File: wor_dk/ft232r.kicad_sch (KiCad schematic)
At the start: 18 parts, among them J401 USB_C_Receptacle_USB2.0_14P, U401 FT232RL

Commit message: wor_dk: add footprints & part info for all capacitors
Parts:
- C401: footprint Capacitor_SMD:C_0201_0603Metric -> Capacitor_SMD:C_0805_2012Metric; Comment (none) -> JLCPCB basic part; LCSC C85930 -> C1710; MPN (none) -> CL21B103KBANNNC; Manufacturer Murata Electronics -> Samsung Electro-Mechanics
- C402, C404: MPN (none) -> GRM033R61E104KE14D
- C403: MPN (none) -> CL10A475KO8NNNC
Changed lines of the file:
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@@
 			)
 		)
-		(property "Footprint" "Capacitor_SMD:C_0201_0603Metric"
+		(property "Footprint" "Capacitor_SMD:C_0805_2012Metric"
 			(at 127.9652 69.85 0)
 			(effects
@@
 			)
 		)
-		(property "Datasheet" "~"
+		(property "Datasheet" "https://wmsc.lcsc.com/wmsc/upload/file/pdf/v2/lcsc/2304140030_Samsung-Electro-Mechanics-CL21B103KBANNNC_C1710.pdf"
 			(at 127 66.04 0)
 			(effects
@@
 			)
 		)
-		(property "Description" "25V 10nF X7R ±10% 0201"
+		(property "Description" "50V 10nF X7R ±10% 0805 MLCC"
 			(at 127 66.04 0)
 			(effects
@@
 			)
 		)
-		(property "LCSC" "C85930"
+		(property "LCSC" "C1710"
 			(at 127 66.04 0)
 			(effects
@@
 			)
 		)
-		(property "Manufacturer" "Murata Electronics"
+		(property "Manufacturer" "Samsung Electro-Mechanics"
 			(at 127 66.04 0)
 			(effects
@@
 		)
 		(property "Part Number" "GRM033R71E103KE14D"
+			(at 127 66.04 0)
+			(effects
+				(font
+					(size 1.27 1.27)
+				)
+				(hide yes)
+			)
+		)
+		(property "Comment" "JLCPCB basic part"
+			(at 127 66.04 0)
+			(effects
+				(font
+					(size 1.27 1.27)
+				)
+				(hide yes)
+			)
+		)
+		(property "MPN" "CL21B103KBANNNC"
 			(at 127 66.04 0)
 			(effects
@@
 			)
 		)
-		(property "Datasheet" "~"
+		(property "Datasheet" "https://wmsc.lcsc.com/wmsc/upload/file/pdf/v2/lcsc/1811081532_Murata-Electronics-GRM033R61E104KE14D_C76939.pdf"
 			(at 154.94 86.36 0)
 			(effects
@@
 		)
 		(property "Part Number" "GRM033R61E104KE14D"
+			(at 154.94 86.36 0)
+			(effects
+				(font
+					(size 1.27 1.27)
+				)
+				(hide yes)
+			)
+		)
+		(property "MPN" "GRM033R61E104KE14D"
 			(at 154.94 86.36 0)
 			(effects
@@
 			)
 		)
-		(property "Datasheet" "~"
+		(property "Datasheet" "https://wmsc.lcsc.com/wmsc/upload/file/pdf/v2/lcsc/1811081532_Murata-Electronics-GRM033R61E104KE14D_C76939.pdf"
 			(at 153.67 66.04 0)
 			(effects
@@
 		)
 		(property "Part Number" "GRM033R61E104KE14D"
+			(at 153.67 66.04 0)
+			(effects
+				(font
+					(size 1.27 1.27)
+				)
+				(hide yes)
+			)
+		)
+		(property "MPN" "GRM033R61E104KE14D"
 			(at 153.67 66.04 0)
 			(effects
@@
 			)
 		)
-		(property "Datasheet" "~"
+		(property "Datasheet" "https://wmsc.lcsc.com/wmsc/upload/file/pdf/v2/lcsc/2304140030_Samsung-Electro-Mechanics-CL10A475KO8NNNC_C19666.pdf"
 			(at 167.64 66.04 0)
 			(effects
@@
 			(at 167.64 66.04 0)
 			(effects
+				(font
+					(size 1.27 1.27)
+				)
+				(hide yes)
+			)
+		)
+		(property "MPN" "CL10A475KO8NNNC"
+			(at 167.64 66.04 0)
+			(effects

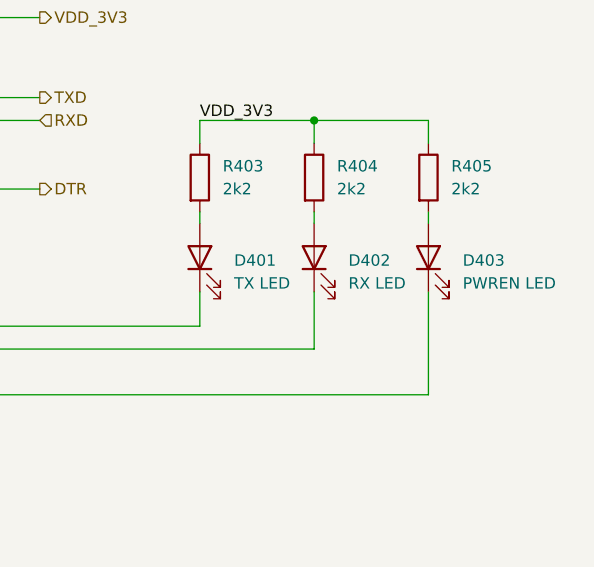
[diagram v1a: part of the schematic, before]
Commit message: wor_dk: add footprints & part info for all diodes & LEDs
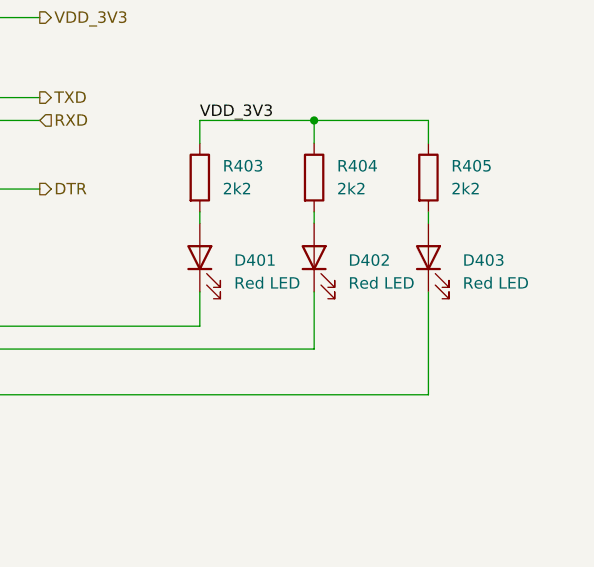
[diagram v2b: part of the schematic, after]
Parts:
- D401: value TX LED -> Red LED; Comment JLCPCB basic part -> FTDI UART TX LED; JLCPCB basic part; MPN (none) -> NCD0805R1
- D402: value RX LED -> Red LED; Comment JLCPCB basic part -> FTDI UART RX LED; JLCPCB basic part; MPN (none) -> NCD0805R1
- D403: value PWREN LED -> Red LED; Comment JLCPCB basic part -> FTDI PWREN LED; JLCPCB basic part; MPN (none) -> NCD0805R1
- D404: MPN (none) -> PRTR5V0U2X
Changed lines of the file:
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@@
 			)
 		)
-		(property "Value" "TX LED"
+		(property "Value" "Red LED"
 			(at 246.38 101.9174 90)
 			(effects
@@
 			)
 		)
-		(property "Description" "Red 0805 Light Emitting Diodes (LED) ROHS"
+		(property "Description" "25mA Colorless transparent lens 67mcd~195mcd -30℃~+85℃ 615nm~630nm Individual diode Red 130° 65mW 1.6V~2.6V 0805 LED Indication - Discrete ROHS"
 			(at 242.57 99.06 0)
 			(effects
@@
 			)
 		)
-		(property "Comment" "JLCPCB basic part"
+		(property "Comment" "FTDI UART TX LED; JLCPCB basic part"
 			(at 242.57 99.06 0)
 			(effects
@@
 		)
 		(property "Part Number" "NCD0805R1"
+			(at 242.57 99.06 0)
+			(effects
+				(font
+					(size 1.27 1.27)
+				)
+				(hide yes)
+			)
+		)
+		(property "MPN" "NCD0805R1"
 			(at 242.57 99.06 0)
 			(effects
@@
 			)
 		)
-		(property "Value" "RX LED"
+		(property "Value" "Red LED"
 			(at 259.08 101.9174 90)
 			(effects
@@
 			)
 		)
-		(property "Description" "Red 0805 Light Emitting Diodes (LED) ROHS"
+		(property "Description" "25mA Colorless transparent lens 67mcd~195mcd -30℃~+85℃ 615nm~630nm Individual diode Red 130° 65mW 1.6V~2.6V 0805 LED Indication - Discrete ROHS"
 			(at 255.27 99.06 0)
 			(effects
@@
 			)
 		)
-		(property "Comment" "JLCPCB basic part"
+		(property "Comment" "FTDI UART RX LED; JLCPCB basic part"
 			(at 255.27 99.06 0)
 			(effects
@@
 		)
 		(property "Part Number" "NCD0805R1"
+			(at 255.27 99.06 0)
+			(effects
+				(font
+					(size 1.27 1.27)
+				)
+				(hide yes)
+			)
+		)
+		(property "MPN" "NCD0805R1"
 			(at 255.27 99.06 0)
 			(effects
@@
 			)
 		)
-		(property "Datasheet" "https://assets.nexperia.com/documents/data-sheet/PRTR5V0U2X.pdf"
+		(property "Datasheet" "https://wmsc.lcsc.com/wmsc/upload/file/pdf/v2/lcsc/2108132230_TECH-PUBLIC-PRTR5V0U2X_C2827688.pdf"
 			(at 104.394 114.3 0)
 			(effects
@@
 			)
 		)
-		(property "Description" ""
+		(property "Description" "SOT-143-4 ESD and Surge Protection (TVS/ESD) ROHS"
 			(at 102.87 114.3 0)
 			(effects
@@
 		)
 		(property "Part Number" "PRTR5V0U2X"
+			(at 102.87 114.3 0)
+			(effects
+				(font
+					(size 1.27 1.27)
+				)
+				(hide yes)
+			)
+		)
+		(property "MPN" "PRTR5V0U2X"
 			(at 102.87 114.3 0)
 			(effects
@@
 			)
 		)
-		(property "Value" "PWREN LED"
+		(property "Value" "Red LED"
 			(at 271.78 101.9174 90)
 			(effects
@@
 			)
 		)
-		(property "Description" "Red 0805 Light Emitting Diodes (LED) ROHS"
+		(property "Description" "25mA Colorless transparent lens 67mcd~195mcd -30℃~+85℃ 615nm~630nm Individual diode Red 130° 65mW 1.6V~2.6V 0805 LED Indication - Discrete ROHS"
 			(at 267.97 99.06 0)
 			(effects
@@
 			)
 		)
-		(property "Comment" "JLCPCB basic part"
+		(property "Comment" "FTDI PWREN LED; JLCPCB basic part"
 			(at 267.97 99.06 0)
 			(effects
@@
 			(at 267.97 99.06 0)
 			(effects
+				(font
+					(size 1.27 1.27)
+				)
+				(hide yes)
+			)
+		)
+		(property "MPN" "NCD0805R1"
+			(at 267.97 99.06 0)
+			(effects

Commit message: wor_dk: add footprints & part info for transistor & ICs
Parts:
- U401: LCSC (none) -> C8690; MPN (none) -> FT232RL-REEL; Manufacturer (none) -> FTDI
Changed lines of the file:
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@@
+			)
+		)
+		(property "LCSC" "C8690"
+			(at 196.85 99.06 0)
+			(effects
+				(font
+					(size 1.27 1.27)
+				)
+				(hide yes)
+			)
+		)
+		(property "MPN" "FT232RL-REEL"
+			(at 196.85 99.06 0)
+			(effects
+				(font
+					(size 1.27 1.27)
+				)
+				(hide yes)
+			)
+		)
+		(property "Manufacturer" "FTDI"
+			(at 196.85 99.06 0)
+			(effects
+				(font
+					(size 1.27 1.27)
+				)
+				(hide yes)
 			)
 		)

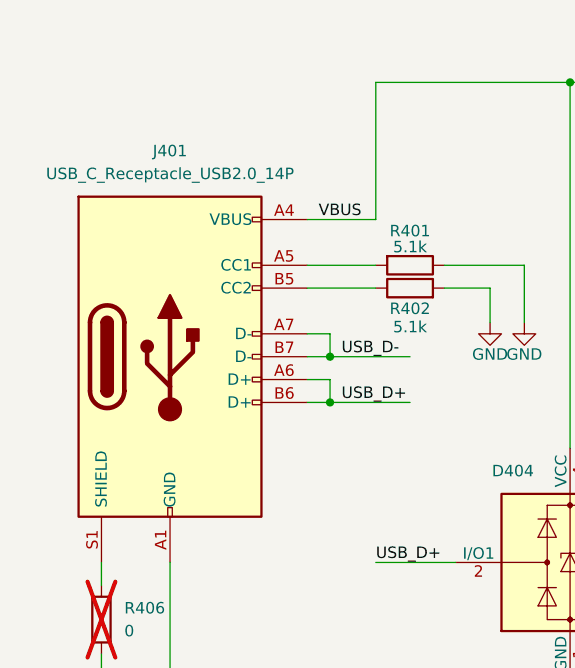
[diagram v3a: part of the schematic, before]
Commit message: wor_dk: add all footprints & part info for connectors
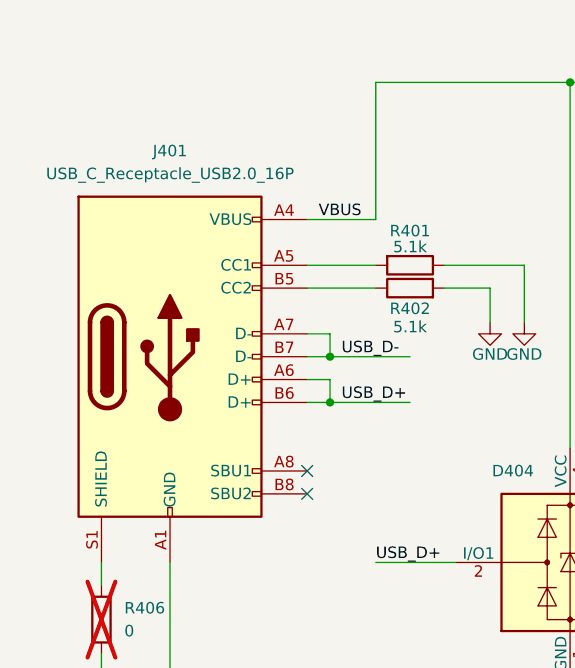
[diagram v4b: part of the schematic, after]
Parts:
- removed J401: USB_C_Receptacle_USB2.0_14P, symbol Connector:USB_C_Receptacle_USB2.0_14P
- added J401: USB_C_Receptacle_USB2.0_16P, Connector_USB:USB_C_Receptacle_GCT_USB4105-xx-A_16P_TopMnt_Horizontal, symbol Connector:USB_C_Receptacle_USB2.0_16P
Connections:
- net GND: now also J401.A1 (GND), J401.A12 (GND), J401.B1 (GND), J401.B12 (GND)
- net USB_D+: now also J401.A6 (D+), J401.B6 (D+)
- net USB_D-: now also J401.A7 (D-), J401.B7 (D-)
- net VBUS: now also J401.A4 (VBUS), J401.A9 (VBUS), J401.B4 (VBUS), J401.B9 (VBUS)
- net at R401.2: now also J401.A5 (CC1)
- net at R402.1: now also J401.B5 (CC2)
- net at R406.1: now also J401.S1 (SHIELD)
- no-connect marks 11 -> 13
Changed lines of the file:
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@@
+	)
+	(no_connect
+		(at 73.66 104.14)
+	)
+	(no_connect
+		(at 73.66 106.68)
 	)
 	(no_connect
@@
 			)
 			(justify left)
+		)
+	)
+	(symbol
+		(lib_id "Connector:USB_C_Receptacle_USB2.0_16P")
+		(at 58.42 91.44 0)
+		(unit 1)
+		(exclude_from_sim no)
+		(in_bom yes)
+		(on_board yes)
+		(dnp no)
+		(fields_autoplaced yes)
+		(property "Reference" "J401"
+			(at 58.42 68.58 0)
+			(effects
+				(font
+					(size 1.27 1.27)
+				)
+			)
+		)
+		(property "Value" "USB_C_Receptacle_USB2.0_16P"
+			(at 58.42 71.12 0)
+			(effects
+				(font
+					(size 1.27 1.27)
+				)
+			)
+		)
+		(property "Footprint" "Connector_USB:USB_C_Receptacle_GCT_USB4105-xx-A_16P_TopMnt_Horizontal"
+			(at 62.23 91.44 0)
+			(effects
+				(font
+					(size 1.27 1.27)
+				)
+				(hide yes)
+			)
+		)
+		(property "Datasheet" "https://www.usb.org/sites/default/files/documents/usb_type-c.zip"
+			(at 62.23 91.44 0)
+			(effects
+				(font
+					(size 1.27 1.27)
+				)
+				(hide yes)
+			)
+		)
+		(property "Description" "USB 2.0-only 16P Type-C Receptacle connector"
+			(at 58.42 91.44 0)
+			(effects
+				(font
+					(size 1.27 1.27)
+				)
+				(hide yes)
+			)
+		)
+		(property "Comment" "To find suitable parts at JLCPCB, search for \"USB Horizontal attachment 16P Female\""
+			(at 58.42 91.44 0)
+			(effects
+				(font
+					(size 1.27 1.27)
+				)
+				(hide yes)
+			)
+		)
+		(property "LCSC" "C393939"
+			(at 58.42 91.44 0)
+			(effects
+				(font
+					(size 1.27 1.27)
+				)
+				(hide yes)
+			)
+		)
+		(property "MPN" "TYPE-C16PIN"
+			(at 58.42 91.44 0)
+			(effects
+				(font
+					(size 1.27 1.27)
+				)
+				(hide yes)
+			)
+		)
+		(property "Manufacturer" "SHOU HAN"
+			(at 58.42 91.44 0)
+			(effects
+				(font
+					(size 1.27 1.27)
+				)
+				(hide yes)
+			)
+		)
+		(pin "B7"
+		)
+		(pin "A6"
+		)
+		(pin "A8"
+		)
+		(pin "A1"
+		)
+		(pin "S1"
+		)
+		(pin "B1"
+		)
+		(pin "B5"
+		)
+		(pin "B9"
+		)
+		(pin "B4"
+		)
+		(pin "B6"
+		)
+		(pin "B8"
+		)
+		(pin "B12"
+		)
+		(pin "A12"
+		)
+		(pin "A4"
+		)
+		(pin "A5"
+		)
+		(pin "A7"
+		)
+		(pin "A9"
+		)
+		(instances
+			(project ""
+				(path "/8d3147eb-060b-4f65-bf42-ed06a58b21ba/711499aa-b4ff-4669-a7c0-a5db1aab8120"
+					(reference "J401")
+					(unit 1)
+				)
+			)
 		)
 	)
@@
 					(unit 1)
 				)
-			)
-		)
-	)
-	(symbol
-		(lib_id "Connector:USB_C_Receptacle_USB2.0_14P")
-		(at 58.42 91.44 0)
-		(unit 1)
-		(exclude_from_sim no)
-		(in_bom yes)
-		(on_board yes)
-		(dnp no)
-		(fields_autoplaced yes)
-		(property "Reference" "J401"
-			(at 58.42 68.58 0)
-			(effects
-				(font
-					(size 1.27 1.27)
-				)
-			)
-		)
-		(property "Value" "USB_C_Receptacle_USB2.0_14P"
-			(at 58.42 71.12 0)
-			(effects
-				(font
-					(size 1.27 1.27)
-				)
-			)
-		)
-		(property "Footprint" ""
-			(at 62.23 91.44 0)
-			(effects
-				(font
-					(size 1.27 1.27)
-				)
-				(hide yes)
-			)
-		)
-		(property "Datasheet" "https://www.usb.org/sites/default/files/documents/usb_type-c.zip"
-			(at 62.23 91.44 0)
-			(effects
-				(font
-					(size 1.27 1.27)
-				)
-				(hide yes)
-			)
-		)
-		(property "Description" "USB 2.0-only 14P Type-C Receptacle connector"
-			(at 58.42 91.44 0)
-			(effects
-				(font
-					(size 1.27 1.27)
-				)
-				(hide yes)
-			)
-		)
-		(pin "A9"
-		)
-		(pin "B6"
-		)
-		(pin "A12"
-		)
-		(pin "B7"
-		)
-		(pin "A1"
-		)
-		(pin "B1"
-		)
-		(pin "S1"
-		)
-		(pin "B9"
-		)
-		(pin "B12"
-		)
-		(pin "B4"
-		)
-		(pin "B5"
-		)
-		(pin "A5"
-		)
-		(pin "A6"
-		)
-		(pin "A4"
-		)
-		(pin "A7"
-		)
-		(instances
-			(project ""
-				(path "/8d3147eb-060b-4f65-bf42-ed06a58b21ba/711499aa-b4ff-4669-a7c0-a5db1aab8120"
-					(reference "J401")
-					(unit 1)
-				)

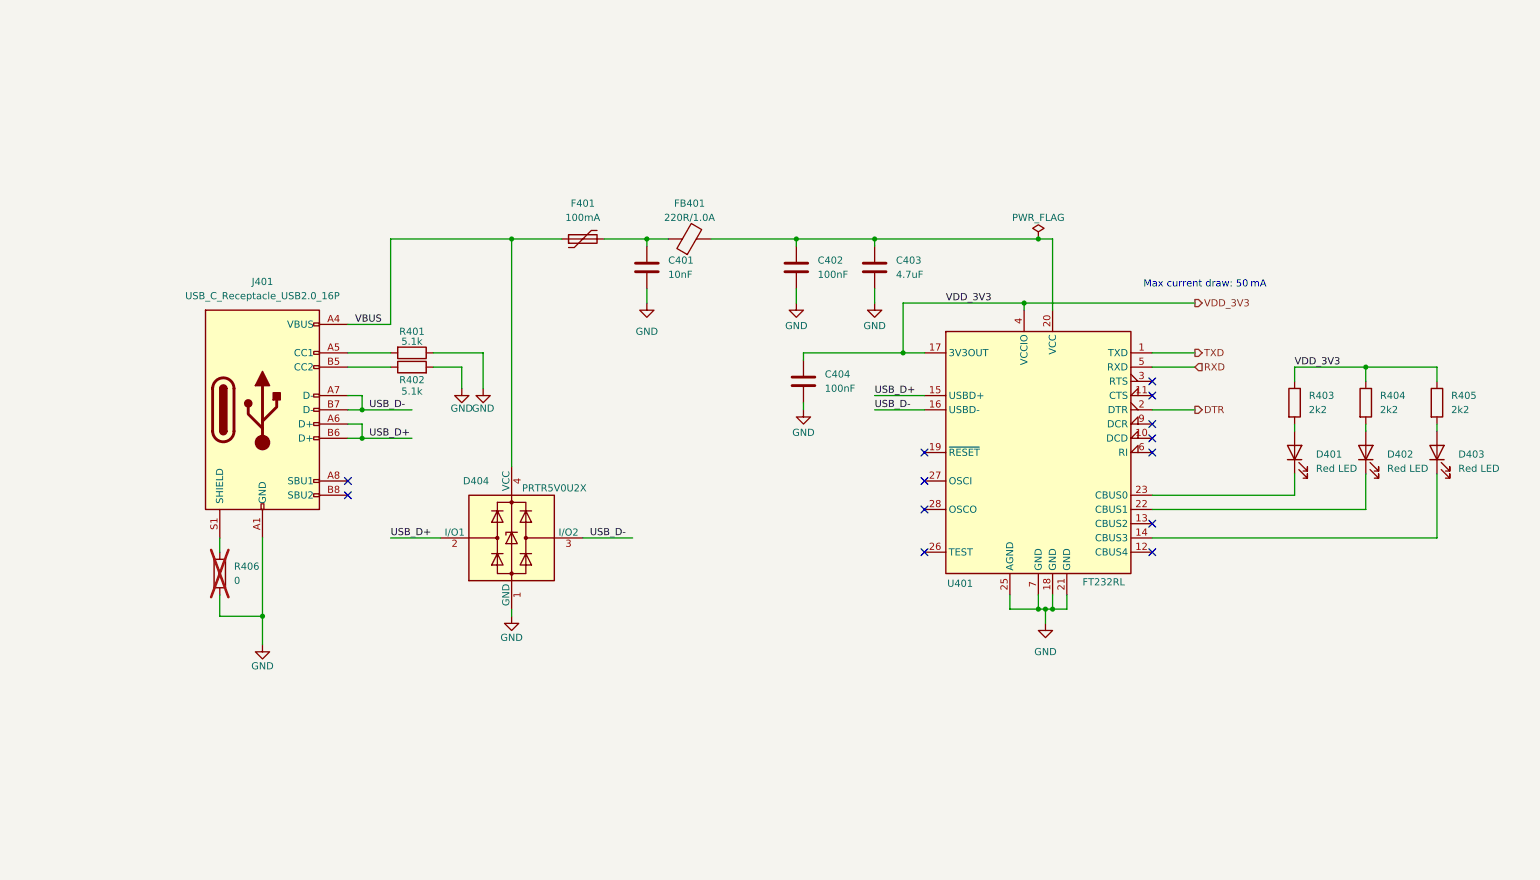
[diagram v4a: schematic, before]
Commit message: wor_dk: add/modify USB data line filtering
- add filtering as suggested by FTDI application note AN232B-06
  section 6.2:
  "Some USB 2.0 hubs appear to be extremely sensitive to noise. A
  glitch on the USB lines can in some cases cause a device to hang.
  This problem can be fixed by adding two 47pF capacitors to ground on
  the USB DP and USB DM lines. These should be located between the 27W
  series resistors and the hub."
- using 33 Ω resistors and 33 pF capacitors instead of 27 Ω and 47 pF
  because parts with these values are already used
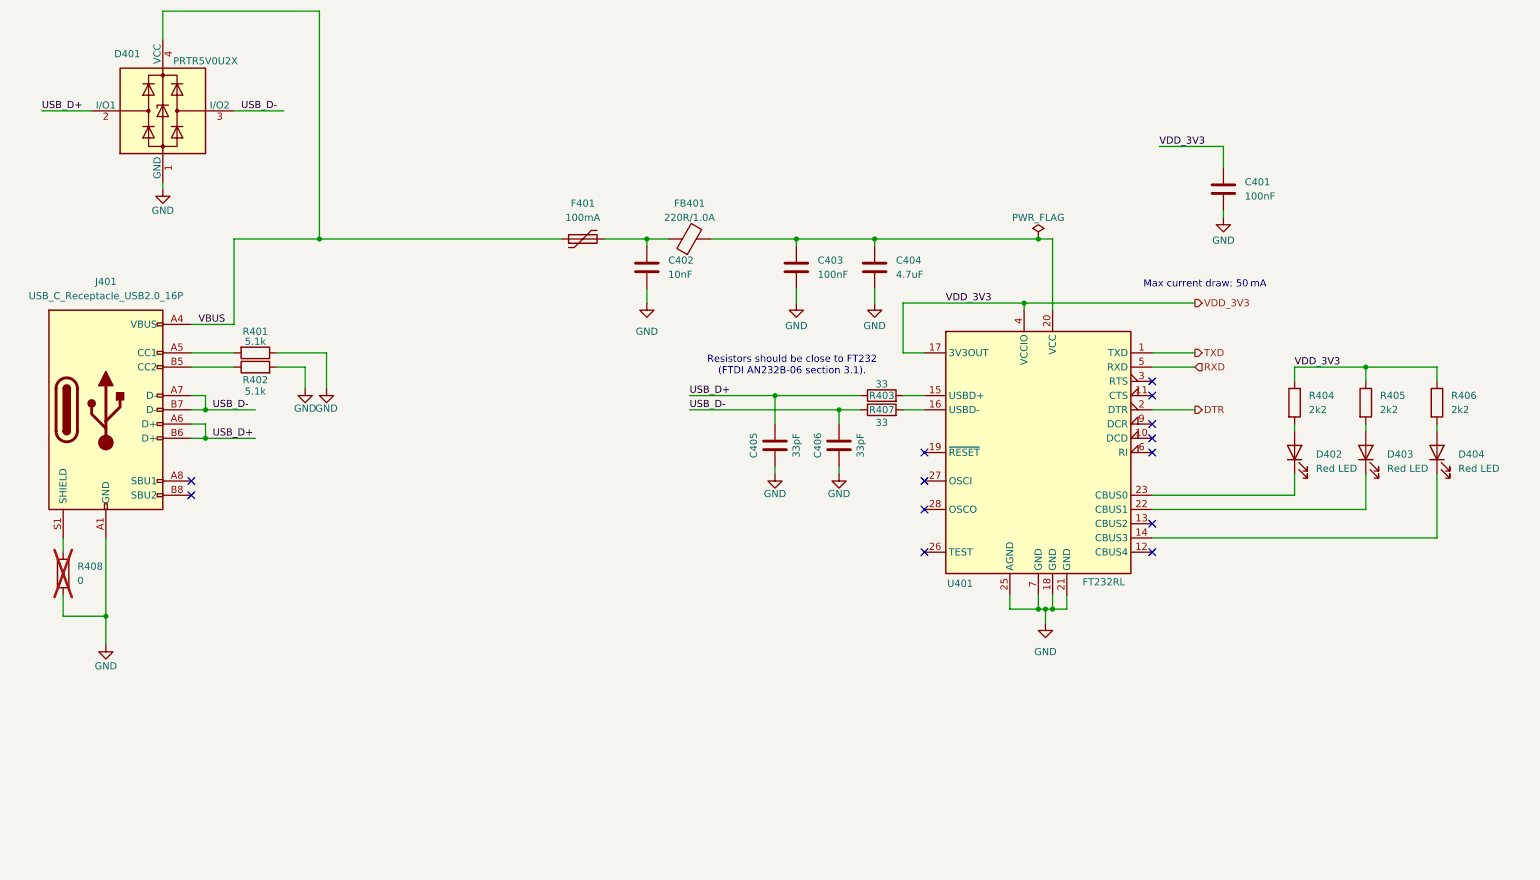
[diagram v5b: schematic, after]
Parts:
- added C405, C406: 33pF, Capacitor_SMD:C_0201_0603Metric, symbol Device:C
- added R403, R407: 33, Resistor_SMD:R_0402_1005Metric, symbol Device:R
- renumbered C404 to C401, C401 to C402, C402 to C403, C403 to C404, D404 to D401, D401 to D402, D402 to D403, D403 to D404, R403 to R404, R404 to R405, R405 to R406, R406 to R408
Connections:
- net GND: now also C405.1, C406.1
- net USB_D+: now also C405.2, R403.1; no longer U401.15 (USBD+)
- net USB_D-: now also C406.2, R407.1; no longer U401.16 (USBD-)
- new net: R403.2, U401.15 (USBD+)
- new net: R407.2, U401.16 (USBD-)
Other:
- note added: "Resistors should be close to FT232 (FTDI AN232B-06 section 3.1)."
- moved on the sheet: C401, D401, J401, R401, R402, R408
